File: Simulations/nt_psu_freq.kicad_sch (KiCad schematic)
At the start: 17 parts, among them K1 DIPxx-1Axx-13x, K2 DIPxx-1Axx-13x, Q1 DMP2008UFG

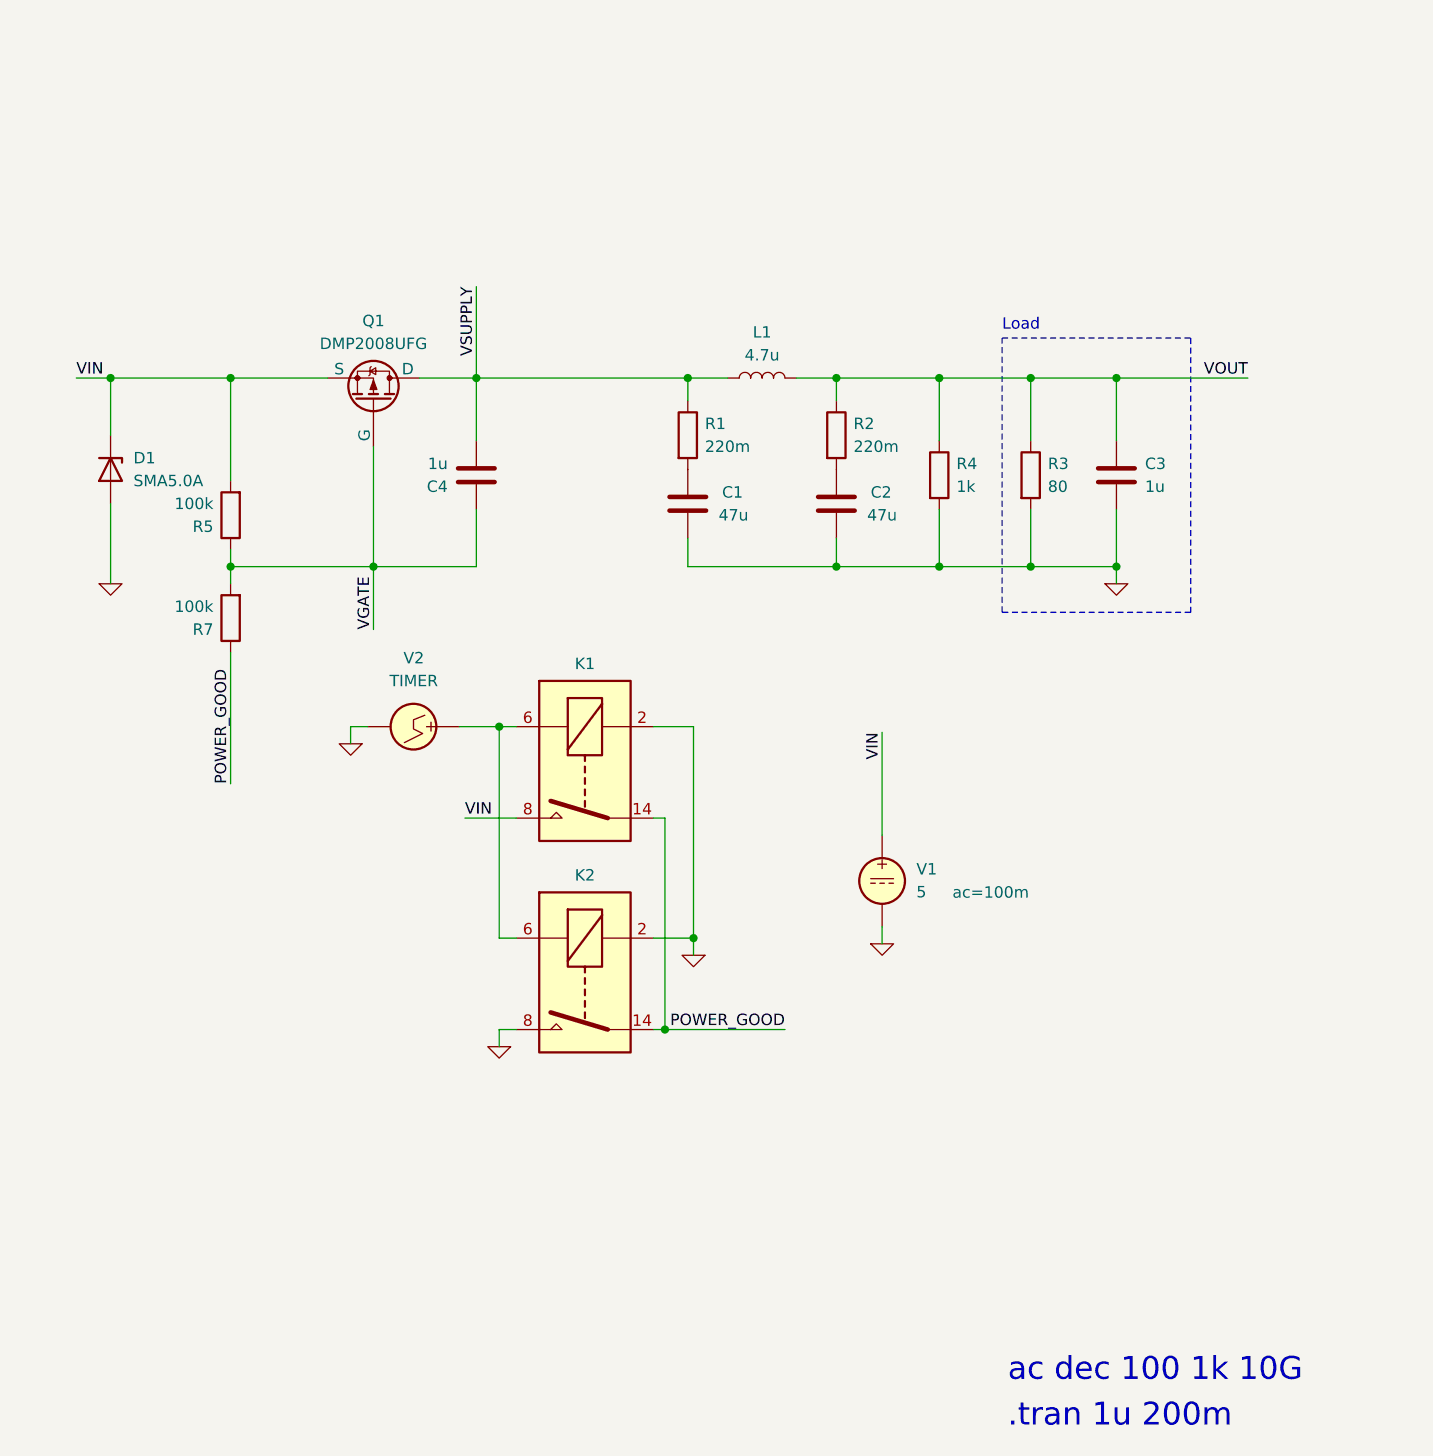
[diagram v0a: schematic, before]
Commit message: fan control and other updates
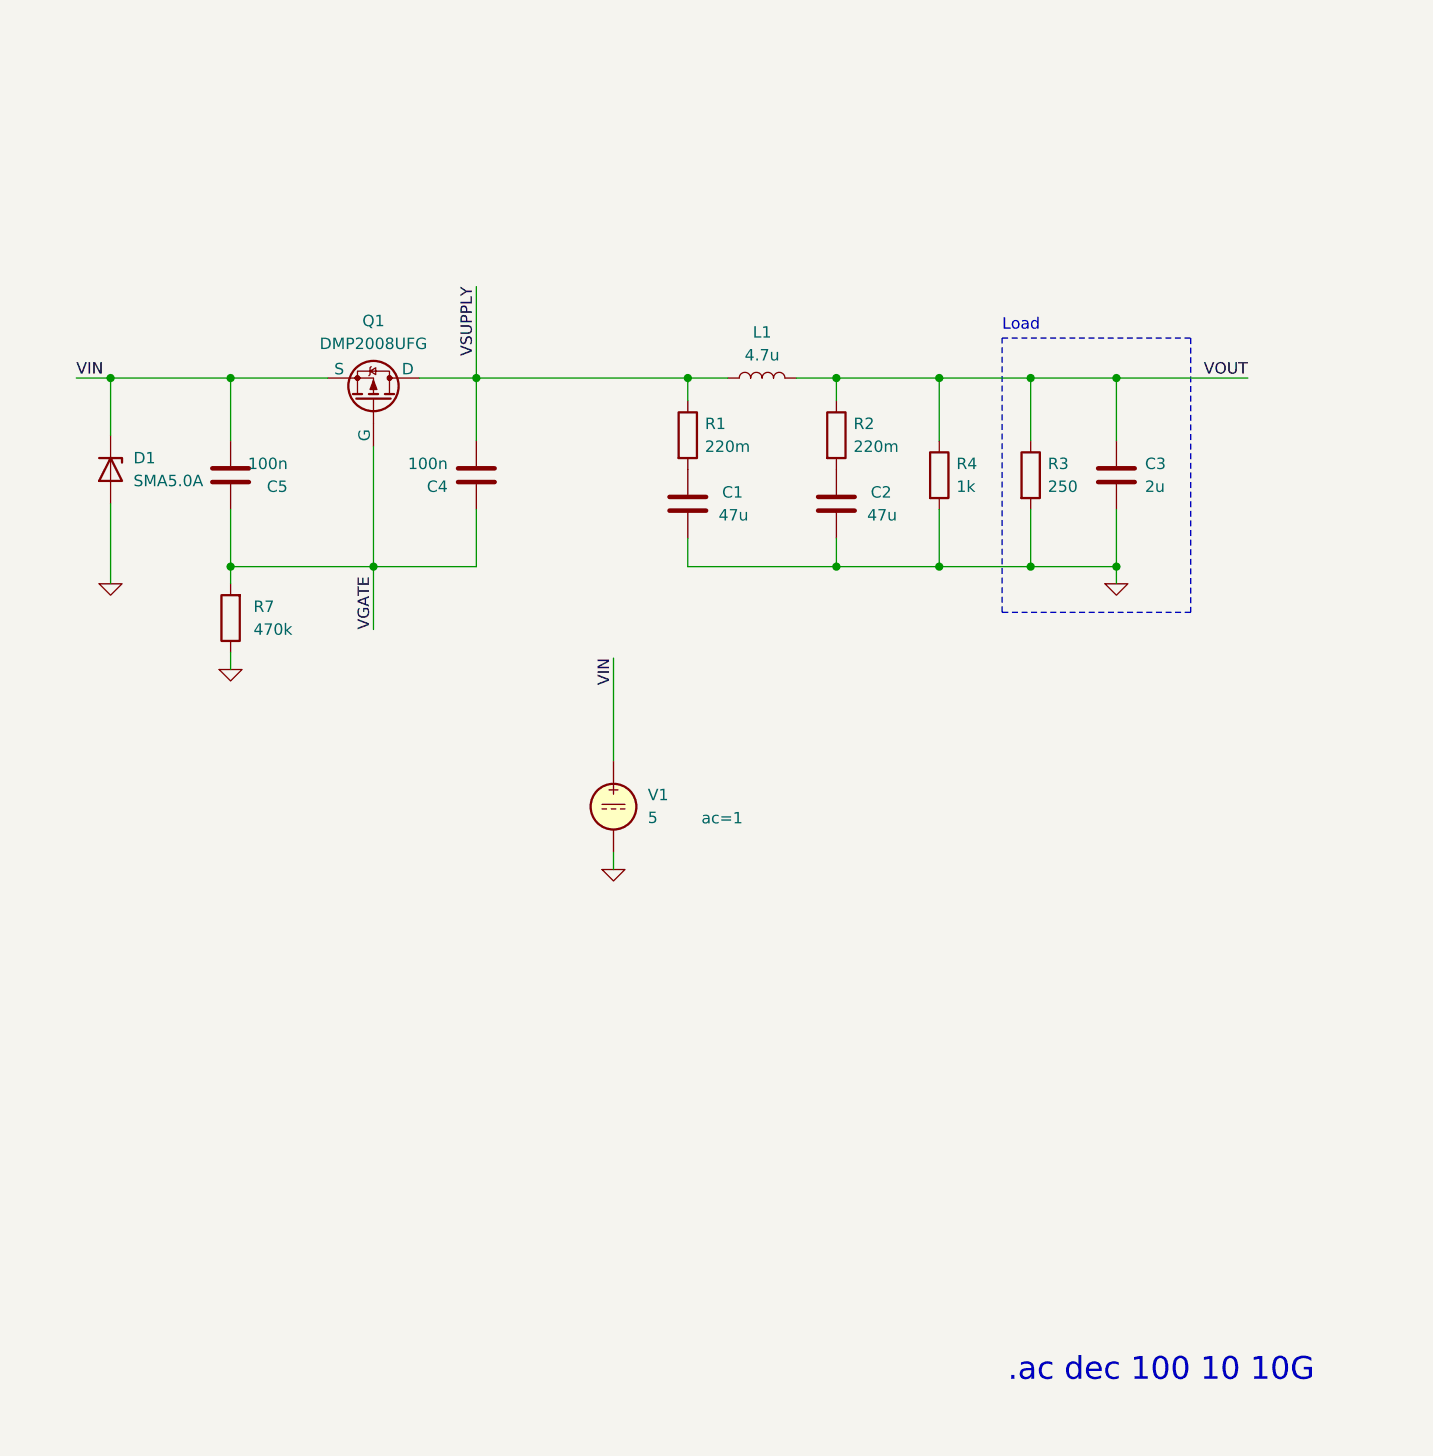
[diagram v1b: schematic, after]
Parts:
- removed K1, K2: DIPxx-1Axx-13x, Relay_THT:Relay_StandexMeder_DIP_LowProfile, symbol Relay:DIPxx-1Axx-13x
- removed R5: 100k, symbol Device:R
- removed V2: TIMER, symbol Simulation_SPICE:VPWL
- added C5: 100n, symbol Device:C
- C3: value 1u -> 2u
- C4: value 1u -> 100n
- R3: value 80 -> 250
- R7: value 100k -> 470k
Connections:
- net POWER_GOOD is gone; now on net 0: R7.1
- net VGATE: now also C5.1
- net VIN: now also C5.2
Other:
- note added: ".ac dec 100 10 10G"
- note removed: ".tran 1u 200m"
- note removed: "ac dec 100 1k 10G"
- moved on the sheet: V1

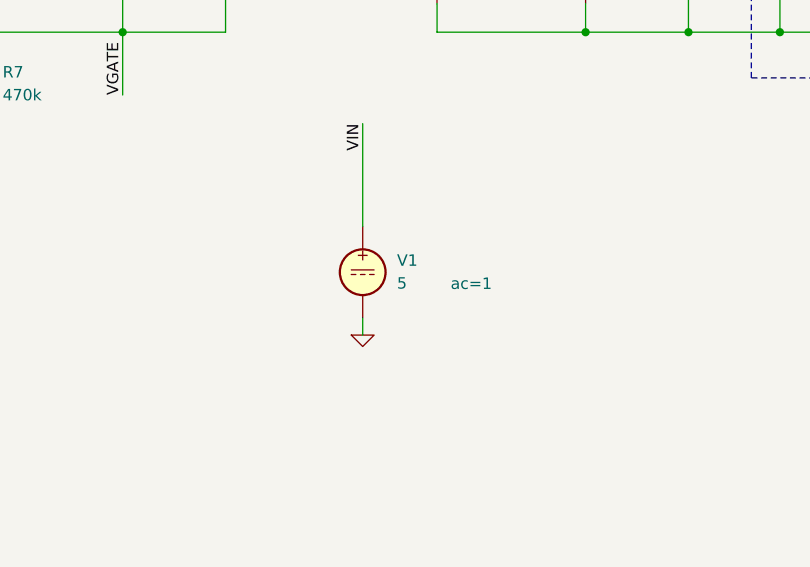
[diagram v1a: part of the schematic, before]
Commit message: switch power to 9V
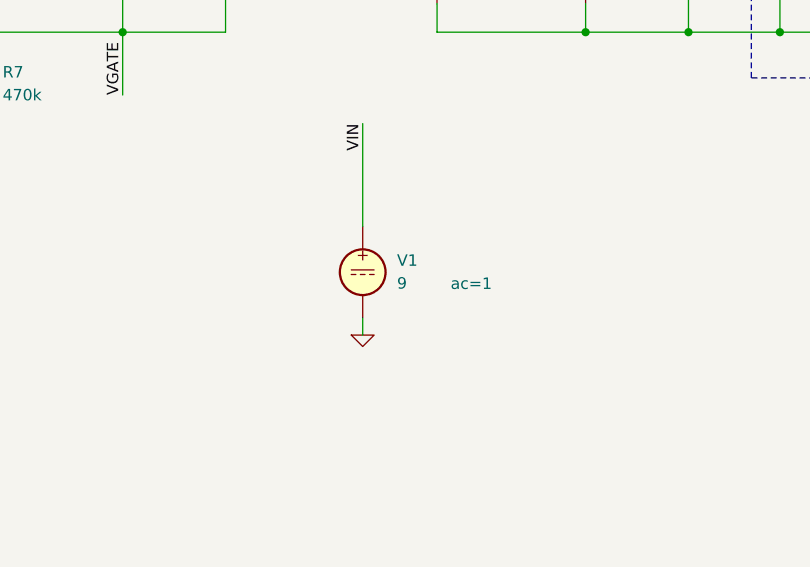
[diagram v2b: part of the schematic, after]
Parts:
- V1: value 5 -> 9
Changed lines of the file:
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@@
       (effects (font (size 1.27 1.27)) (justify left))
     )
-    (property "Value" "5" (at 140.335 109.1842 0)
+    (property "Value" "9" (at 140.335 109.1842 0)
       (effects (font (size 1.27 1.27)) (justify left))
     )

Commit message: fine tuning before layout
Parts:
- removed D1: SMA5.0A, symbol Device:D_Zener
- added C6: ${SIM.PARAMS}, symbol Device:C_Polarized
- added C7, C8: ${SIM.PARAMS}, symbol Device:C
- added R5, R6: 100m, symbol Device:R
- added U1: LM1084-5.0, symbol Regulator_Linear:LM1084-5.0
- added U2: TLV70950, symbol Regulator_Linear:LM1084-5.0
- C3: value 2u -> ${SIM.PARAMS}
- R1, R2: value 220m -> 100m
- R3: value 250 -> 50
- R4: value 1k -> 50
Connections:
- net 0: now also C6.2, C7.2, C8.2, U1.1 (GND), U2.1 (GND)
- removed net VOUT: C3.1, L1.2, R2.1, R3.1, R4.1
- new net: C7.1, R6.2
- new net: C3.1, R5.2
- new net VFILTERED: L1.2, R2.1, R5.1, R6.1, U1.3 (VI), U2.3 (VI)
- new net VOUT1: C6.1, R3.1, U1.2 (VO)
- new net VOUT2: C8.1, R4.1, U2.2 (VO)
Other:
- moved on the sheet: C1, C4, C5, L1, Q1, R3, R7, V1
